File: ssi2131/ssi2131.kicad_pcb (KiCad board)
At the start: 2 copper layers, 50.4 x 108 mm, 25 parts, among them J1 Saw Out, J2 Pulse Out, J3 Tri Out, J4 Hard Sync, J5 Soft Sync, J7 16-Pin uZeus Power Header, J9 Expo Freq, U1 SSI2131, U2 LM4040DBZ-2.5

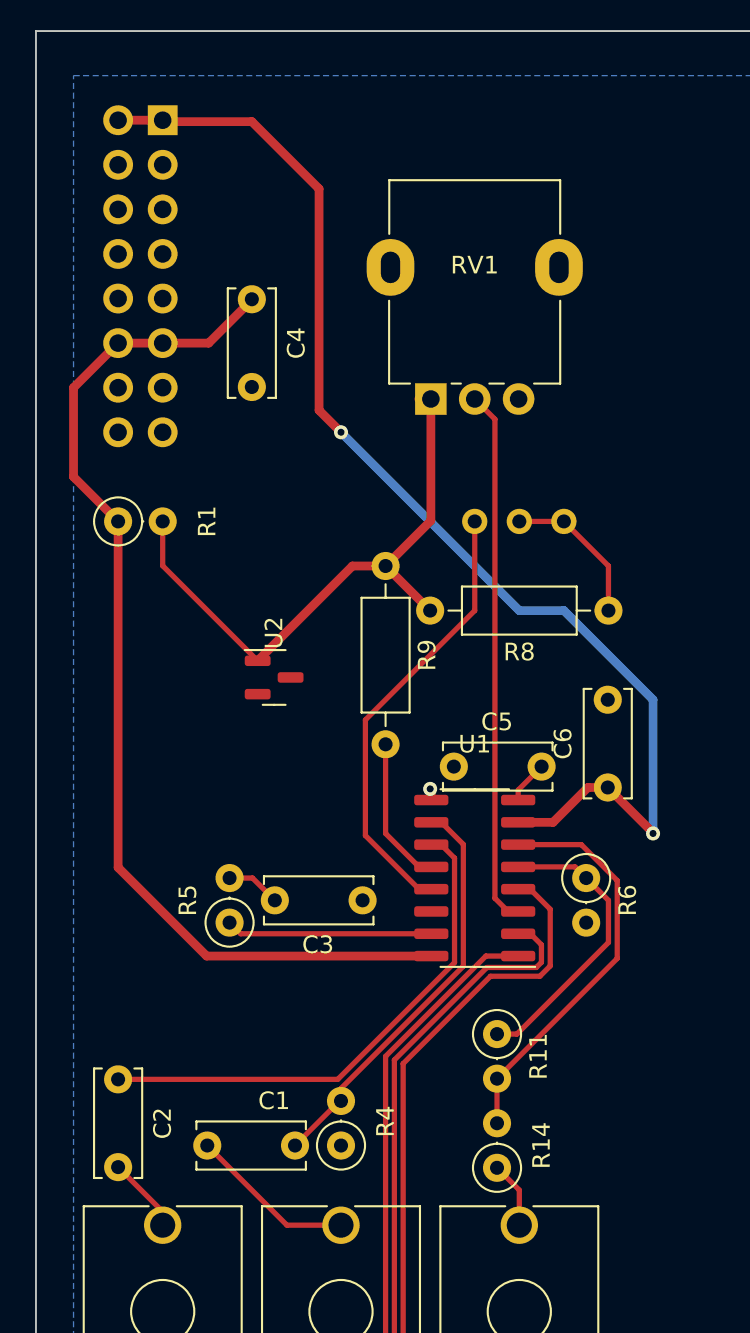
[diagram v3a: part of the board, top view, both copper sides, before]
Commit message: rework PCB layout, but more
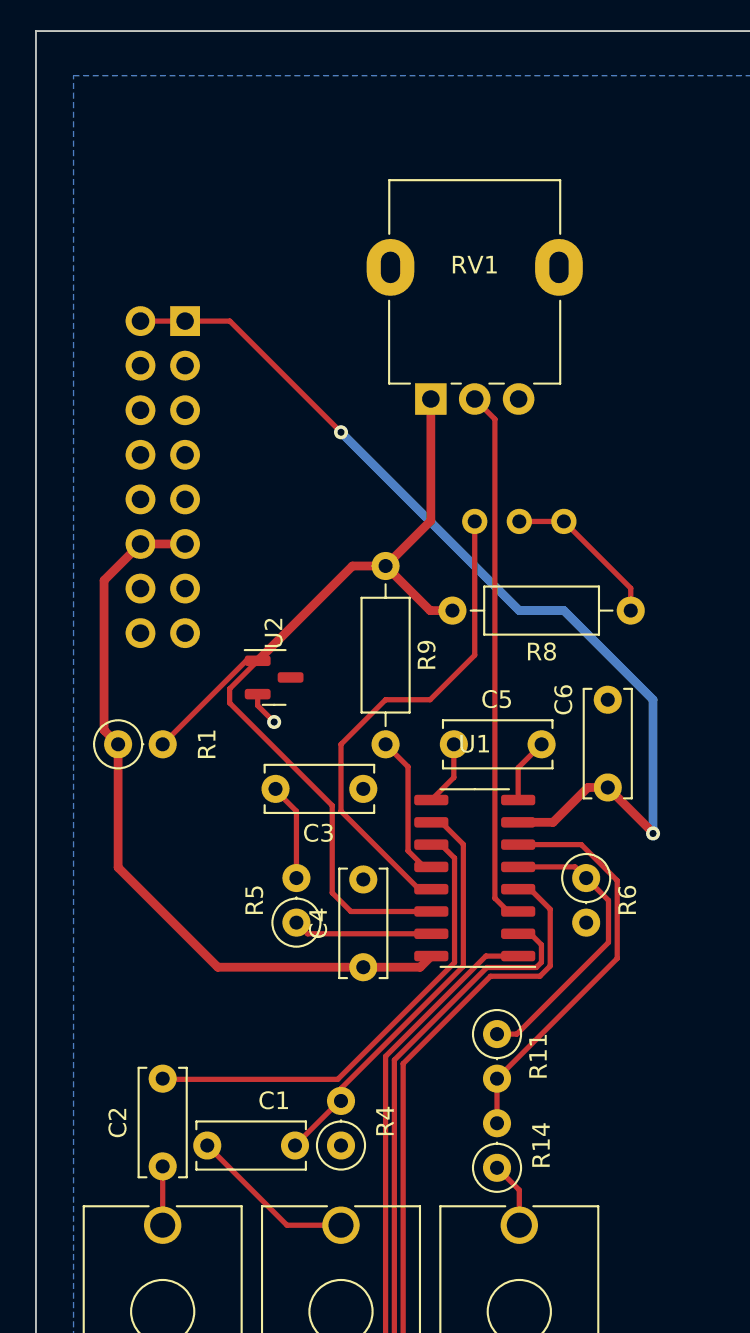
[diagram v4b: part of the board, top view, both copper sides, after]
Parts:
- moved C4 28.8 mm to (174.0, 81.4), turned to -90 degrees
- moved R1 12.7 mm to (160.0, 73.7)
- moved J7 11.5 mm to (163.8, 49.5)
- moved C3 6.35 mm to (174.0, 76.2)
- moved R5 3.81 mm to (170.2, 83.8)
- moved C2 2.54 mm to (162.6, 92.7)
- moved C5 1.27 mm to (184.2, 73.7)
- moved R8 1.27 mm to (189.2, 66.0)
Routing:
- net VREF: track 35.3 -> 54.7 mm
- net +5V: track 60.6 -> 42.6 mm
- net -12V: track 68.8 -> 55.4 mm
- net GND: track 0.66 -> 5.69 mm
- net BWComp: track 11.8 -> 7.95 mm
- net ExpoScale: track 25.5 -> 28.1 mm
- net Net-(R5-Pad2): track 3.11 -> 5.66 mm
- net SoftSync: track 29.5 -> 27.0 mm
- net TCAP: track 2.46 -> 3.73 mm
- net Net-(C2-Pad2): track 4.36 -> 3.35 mm
- net Net-(R8-Pad1): track 8.67 -> 9.20 mm
